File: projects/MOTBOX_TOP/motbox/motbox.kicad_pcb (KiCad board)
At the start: 2 copper layers, 89.9 x 67 mm, 28 parts, among them J1 12V IN, J2 Manual EN, J3 OBS_IR_TX, J4 OP_CL_OBS_DET_LED, J5 OBS IR RX, J6 Open Close Done, J7 Motor, P1 Digital, P2 Analog, P3 CONN_01X01, P4 CONN_01X01, P5 CONN_01X01, P6 CONN_01X01, U1 LM2575-5.0BU, U2 LM393, U3 L293D

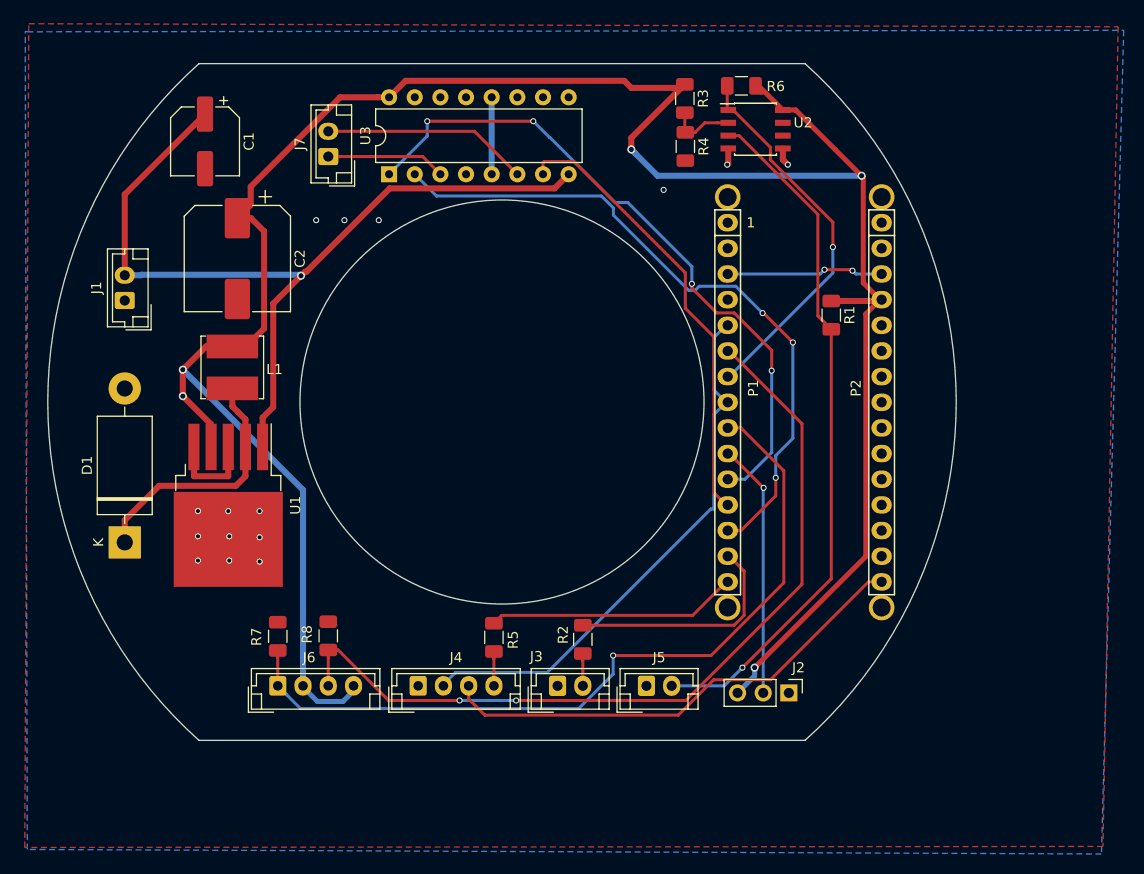
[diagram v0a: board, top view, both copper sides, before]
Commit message: Changes for the motbox with promini instead of nano
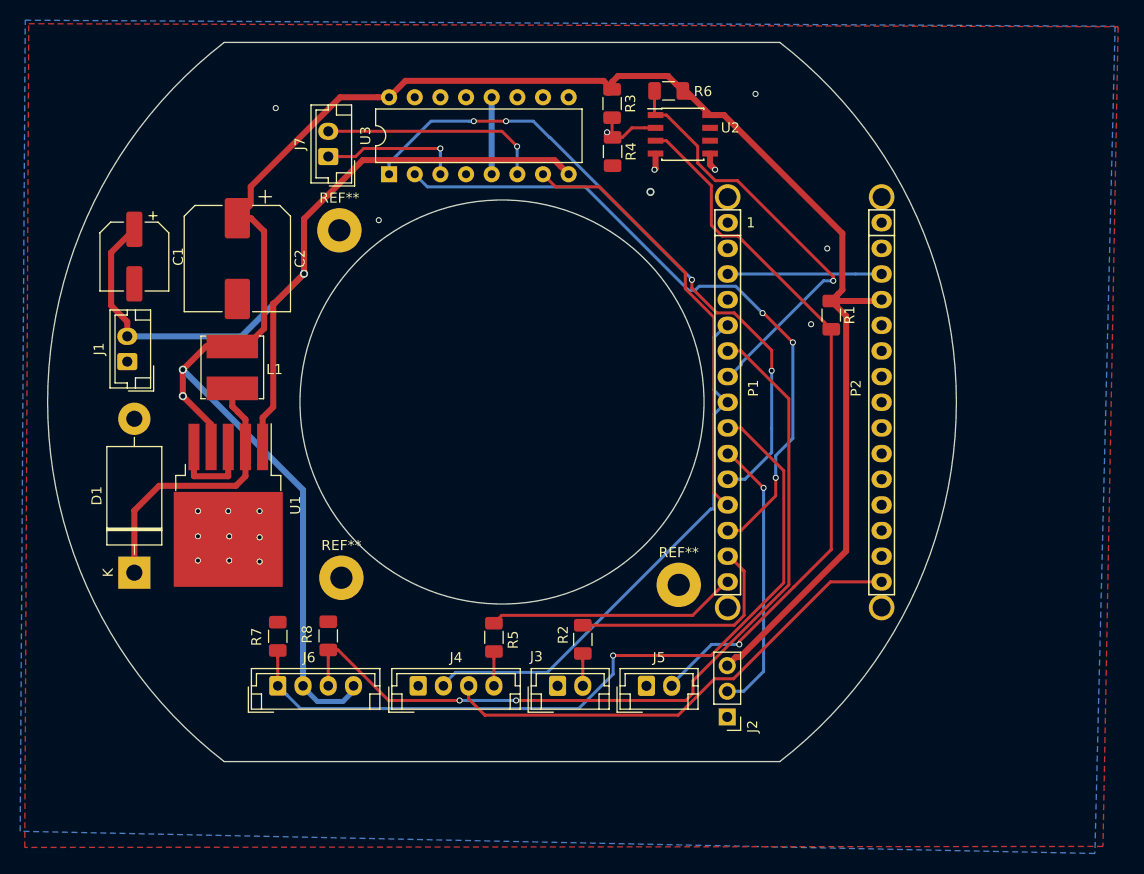
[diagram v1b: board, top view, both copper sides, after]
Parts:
- added REF**: MountingHole_2.2mm_M2_Pad, MountingHole:MountingHole_2.2mm_M2_Pad, F.Cu at (101.2, 106.4)
- added REF**: MountingHole_2.2mm_M2_Pad, MountingHole:MountingHole_2.2mm_M2_Pad, F.Cu at (101.0, 72.0)
- added REF**: MountingHole_2.2mm_M2_Pad, MountingHole:MountingHole_2.2mm_M2_Pad, F.Cu at (134.6, 107.1)
- moved C1 13.4 mm to (80.7, 74.6)
- moved R6 7.22 mm to (133.6, 58.2)
- moved R3 7.22 mm to (128.0, 59.5)
- moved R4 7.22 mm to (128.1, 64.2)
- moved U2 7.22 mm to (135.0, 62.5)
- moved J2 6.55 mm to (139.4, 120.2), turned to 180 degrees
- moved J1 6.06 mm to (80.0, 85.0)
- moved D1 3.15 mm to (80.7, 105.9)
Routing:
- net +5V: track 241.9 -> 209.7 mm, vias 5 -> 2
- net /4: track 37.8 -> 43.0 mm
- net Net-(D1-Pad1): track 25.2 -> 27.8 mm
- net /7: track 25.3 -> 27.6 mm
- net Net-(J7-Pad1): track 11.8 -> 14.0 mm, vias 0 -> 1
- net Net-(J5-Pad2): track 69.4 -> 71.4 mm
- net /9: track 44.6 -> 42.9 mm
- net Net-(J7-Pad2): track 20.5 -> 22.1 mm, vias 0 -> 1
- net /8: track 67.1 -> 66.1 mm
- net /Reset: track 15.6 -> 15.2 mm, vias 2 -> 0
- net GND: vias 15 -> 17
- net Net-(R3-Pad2): vias 0 -> 1
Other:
- board size 89.9 x 67 mm -> 90 x 71.2 mm
